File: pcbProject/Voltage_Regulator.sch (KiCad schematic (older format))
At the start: 4 parts, among them U1 LD1117S50TR

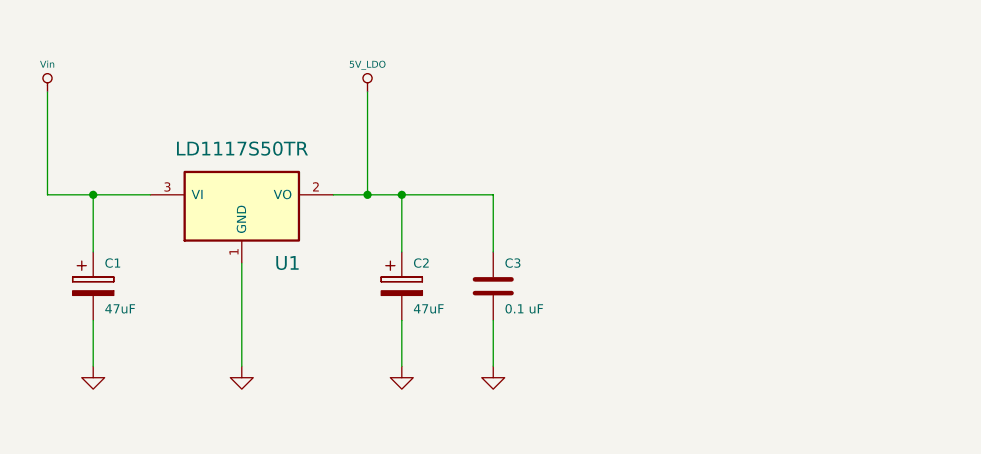
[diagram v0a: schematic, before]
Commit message: bestellijst+pcbvoltageregulator aangepast
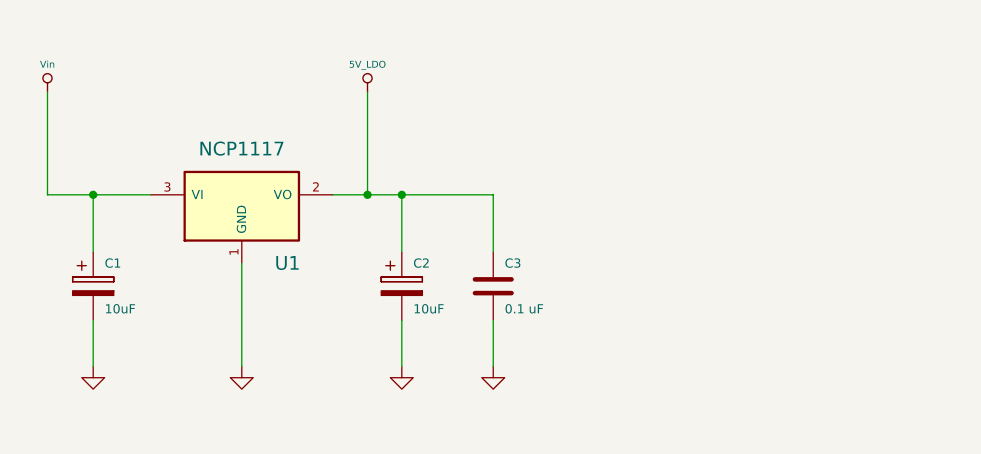
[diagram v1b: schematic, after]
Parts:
- C1, C2: value 47uF -> 10uF
- U1: value LD1117S50TR -> NCP1117
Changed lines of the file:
@@
 P 5275 4175
 F 0 "C1" H 5325 4275 40  0000 L CNN
-F 1 "47uF" H 5325 4075 40  0000 L CNN
+F 1 "10uF" H 5325 4075 40  0000 L CNN
 F 2 "~" H 5375 4025 30  0000 C CNN
 F 3 "http://images.ihscontent.net/vipimages/VipMasterIC/IC/BEYS/BEYSS04513/BEYSS04513-1.pdf" H 5275 4175 300 0001 C CNN
@@
 P 6625 4175
 F 0 "C2" H 6675 4275 40  0000 L CNN
-F 1 "47uF" H 6675 4075 40  0000 L CNN
+F 1 "10uF" H 6675 4075 40  0000 L CNN
 F 2 "~" H 6725 4025 30  0000 C CNN
 F 3 "http://images.ihscontent.net/vipimages/VipMasterIC/IC/BEYS/BEYSS04513/BEYSS04513-1.pdf" H 6625 4175 300 0001 C CNN
@@
 P 5925 3825
 F 0 "U1" H 6125 3575 60  0000 C CNN
-F 1 "LD1117S50TR" H 5925 4075 60  0000 C CNN
-F 2 "" H 5925 3825 60  0000 C CNN
+F 1 "NCP1117" H 5925 4075 60  0000 C CNN
+F 2 "" H 5925 3825 60  0001 C CNN
 F 3 "http://www.st.com/st-web-ui/static/active/en/resource/technical/document/datasheet/CD00000544.pdf" H 5925 3825 60  0001 C CNN
 F 4 "5 V FIXED POSITIVE LDO REGULATOR, 1.2 V DROPOUT, PDSO3, ROHS COMPLIANT, SOT-223, 4 PIN" H 5925 3825 60  0001 C CNN "Characteristics"

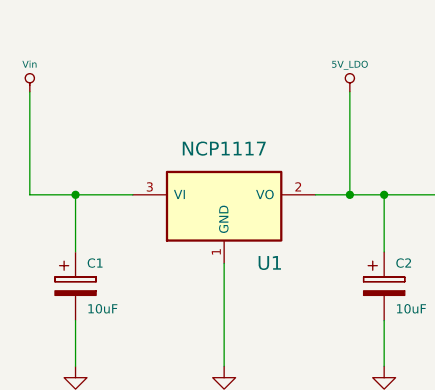
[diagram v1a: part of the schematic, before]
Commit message: TekeningAfenGecontroleerd
nu nog componenten toevoegen en routen
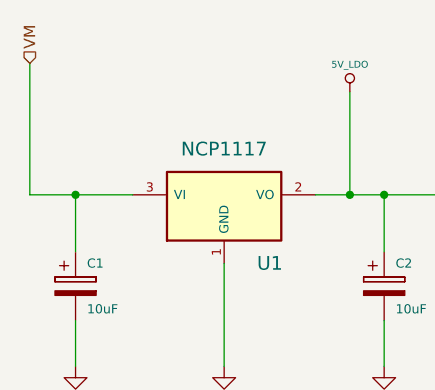
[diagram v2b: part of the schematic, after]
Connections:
- net Vin renamed VM
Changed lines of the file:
@@
-$EndComp
-$Comp
-L Arduino_Uno_R3_From_Scratch:Vin #PWR07
-U 1 1 55E958C6
-P 5075 3325
-AR Path="/55E958C6" Ref="#PWR07"  Part="1"
-AR Path="/55CCFEA2/55E958C6" Ref="#PWR01"  Part="1"
-F 0 "#PWR01" H 5075 3415 20  0001 C CNN
-F 1 "Vin" H 5075 3445 30  0000 C CNN
-F 2 "~" H 5075 3325 60  0000 C CNN
-F 3 "~" H 5075 3325 60  0000 C CNN
-	1    5075 3325
-	1    0    0    -1
 $EndComp
 $Comp
@@
 Wire Wire Line
 	6475 3325 6475 3775
-Wire Wire Line
-	5075 3325 5075 3775
 $Comp
 L Arduino_Uno_R3_From_Scratch-rescue:LD1117S50TR U1
@@
 Wire Wire Line
 	6325 3775 6475 3775
+Text HLabel 5075 3200 1    50   Input ~ 0
+VM
+Wire Wire Line
+	5075 3200 5075 3775
 $EndSCHEMATC

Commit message: deel1routingpcb
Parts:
- C1, C2: footprint ~ -> Capacitor_SMD:CP_Elec_6.3x7.7
- C3: footprint ~ -> Capacitor_SMD:C_1206_3216Metric
- U1: footprint (none) -> LD1117S33CTR:SOT223
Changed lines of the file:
@@
 F 0 "C1" H 5325 4275 40  0000 L CNN
 F 1 "10uF" H 5325 4075 40  0000 L CNN
-F 2 "~" H 5375 4025 30  0000 C CNN
+F 2 "Capacitor_SMD:CP_Elec_6.3x7.7" H 5375 4025 30  0000 C CNN
 F 3 "http://images.ihscontent.net/vipimages/VipMasterIC/IC/BEYS/BEYSS04513/BEYSS04513-1.pdf" H 5275 4175 300 0001 C CNN
 F 4 "CAPACITOR, ALUMINUM ELECTROLYTIC, NON SOLID, POLARIZED, 50 V, 47 uF, SURFACE MOUNT, 3131, CHIP, ROHS COMPLIANT" H 5275 4175 60  0001 C CNN "Characteristics"
@@
 F 0 "C3" H 7075 4275 40  0000 L CNN
 F 1 "0.1 uF" H 7075 4075 40  0000 L CNN
-F 2 "~" H 7063 4025 30  0000 C CNN
+F 2 "Capacitor_SMD:C_1206_3216Metric" H 7063 4025 30  0000 C CNN
 F 3 "http://images.ihscontent.net/vipimages/VipMasterIC/IC/KEME/KEMES10043/KEMES10043-1.pdf" H 7025 4175 60  0001 C CNN
 F 4 "CAPACITOR, CERAMIC, MULTILAYER, 100 V, X7R, 0.1 uF, SURFACE MOUNT, 0805, CHIP, ROHS COMPLIANT" H 7025 4175 60  0001 C CNN "Characteristics"
@@
 F 0 "C2" H 6675 4275 40  0000 L CNN
 F 1 "10uF" H 6675 4075 40  0000 L CNN
-F 2 "~" H 6725 4025 30  0000 C CNN
+F 2 "Capacitor_SMD:CP_Elec_6.3x7.7" H 6725 4025 30  0000 C CNN
 F 3 "http://images.ihscontent.net/vipimages/VipMasterIC/IC/BEYS/BEYSS04513/BEYSS04513-1.pdf" H 6625 4175 300 0001 C CNN
 F 4 "CAPACITOR, ALUMINUM ELECTROLYTIC, NON SOLID, POLARIZED, 50 V, 47 uF, SURFACE MOUNT, 3131, CHIP, ROHS COMPLIANT" H 6625 4175 60  0001 C CNN "Characteristics"
@@
 F 0 "U1" H 6125 3575 60  0000 C CNN
 F 1 "NCP1117" H 5925 4075 60  0000 C CNN
-F 2 "" H 5925 3825 60  0001 C CNN
+F 2 "LD1117S33CTR:SOT223" H 5925 3825 60  0001 C CNN
 F 3 "http://www.st.com/st-web-ui/static/active/en/resource/technical/document/datasheet/CD00000544.pdf" H 5925 3825 60  0001 C CNN
 F 4 "5 V FIXED POSITIVE LDO REGULATOR, 1.2 V DROPOUT, PDSO3, ROHS COMPLIANT, SOT-223, 4 PIN" H 5925 3825 60  0001 C CNN "Characteristics"

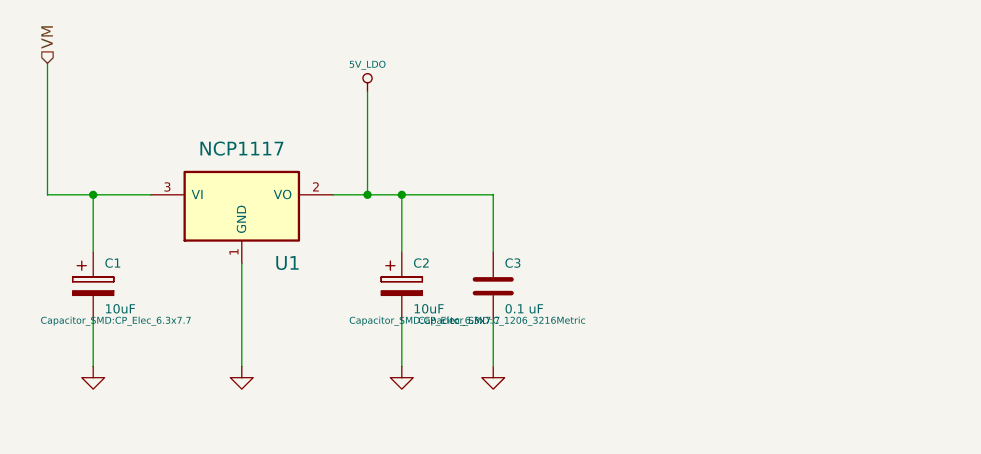
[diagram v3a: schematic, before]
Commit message: PCB versie3
Aanpassingen tips coach --> veel gewijzigd
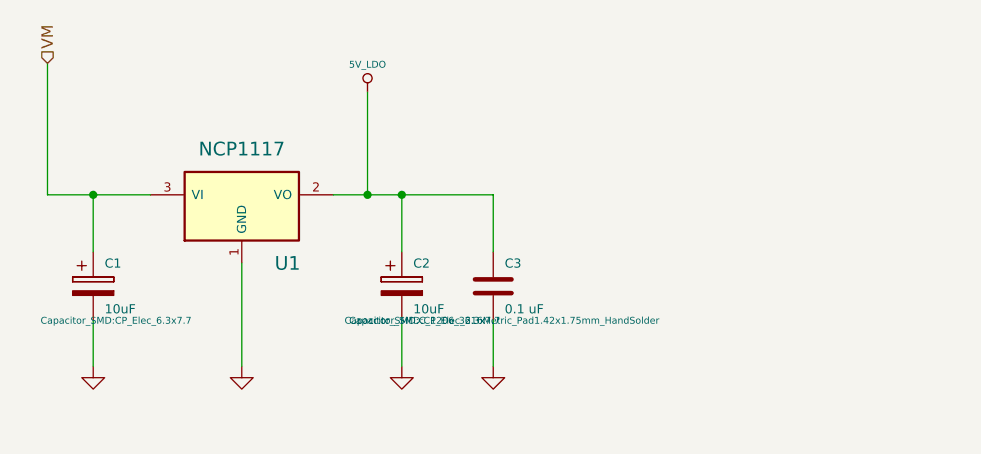
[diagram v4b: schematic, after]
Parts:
- C3: footprint Capacitor_SMD:C_1206_3216Metric -> Capacitor_SMD:C_1206_3216Metric_Pad1.42x1.75mm_HandSolder
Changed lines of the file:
@@
 F 0 "C3" H 7075 4275 40  0000 L CNN
 F 1 "0.1 uF" H 7075 4075 40  0000 L CNN
-F 2 "Capacitor_SMD:C_1206_3216Metric" H 7063 4025 30  0000 C CNN
+F 2 "Capacitor_SMD:C_1206_3216Metric_Pad1.42x1.75mm_HandSolder" H 7063 4025 30  0000 C CNN
 F 3 "http://images.ihscontent.net/vipimages/VipMasterIC/IC/KEME/KEMES10043/KEMES10043-1.pdf" H 7025 4175 60  0001 C CNN
 F 4 "CAPACITOR, CERAMIC, MULTILAYER, 100 V, X7R, 0.1 uF, SURFACE MOUNT, 0805, CHIP, ROHS COMPLIANT" H 7025 4175 60  0001 C CNN "Characteristics"

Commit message: verslag
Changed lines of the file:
@@
 F 0 "C1" H 5325 4275 40  0000 L CNN
 F 1 "10uF" H 5325 4075 40  0000 L CNN
-F 2 "Capacitor_SMD:CP_Elec_6.3x7.7" H 5375 4025 30  0000 C CNN
+F 2 "Capacitor_SMD:CP_Elec_6.3x7.7" H 7900 3950 30  0000 C CNN
 F 3 "http://images.ihscontent.net/vipimages/VipMasterIC/IC/BEYS/BEYSS04513/BEYSS04513-1.pdf" H 5275 4175 300 0001 C CNN
 F 4 "CAPACITOR, ALUMINUM ELECTROLYTIC, NON SOLID, POLARIZED, 50 V, 47 uF, SURFACE MOUNT, 3131, CHIP, ROHS COMPLIANT" H 5275 4175 60  0001 C CNN "Characteristics"
@@
 F 0 "C3" H 7075 4275 40  0000 L CNN
 F 1 "0.1 uF" H 7075 4075 40  0000 L CNN
-F 2 "Capacitor_SMD:C_1206_3216Metric_Pad1.42x1.75mm_HandSolder" H 7063 4025 30  0000 C CNN
+F 2 "Capacitor_SMD:C_1206_3216Metric_Pad1.42x1.75mm_HandSolder" H 8225 3550 30  0000 C CNN
 F 3 "http://images.ihscontent.net/vipimages/VipMasterIC/IC/KEME/KEMES10043/KEMES10043-1.pdf" H 7025 4175 60  0001 C CNN
 F 4 "CAPACITOR, CERAMIC, MULTILAYER, 100 V, X7R, 0.1 uF, SURFACE MOUNT, 0805, CHIP, ROHS COMPLIANT" H 7025 4175 60  0001 C CNN "Characteristics"
@@
 F 0 "C2" H 6675 4275 40  0000 L CNN
 F 1 "10uF" H 6675 4075 40  0000 L CNN
-F 2 "Capacitor_SMD:CP_Elec_6.3x7.7" H 6725 4025 30  0000 C CNN
+F 2 "Capacitor_SMD:CP_Elec_6.3x7.7" H 7875 3825 30  0000 C CNN
 F 3 "http://images.ihscontent.net/vipimages/VipMasterIC/IC/BEYS/BEYSS04513/BEYSS04513-1.pdf" H 6625 4175 300 0001 C CNN
 F 4 "CAPACITOR, ALUMINUM ELECTROLYTIC, NON SOLID, POLARIZED, 50 V, 47 uF, SURFACE MOUNT, 3131, CHIP, ROHS COMPLIANT" H 6625 4175 60  0001 C CNN "Characteristics"
